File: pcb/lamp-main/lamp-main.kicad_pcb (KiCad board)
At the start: 2 copper layers, 29 parts, among them IC1 ATMEGA328P, IC2 DNP(LM1117_3.3), P1 VLED_IN, P10 VCC, P2 AVR_ISP, P3 SERIAL, P4 LEDSTACK, P5 LEDSTACK, P6 LEDSTACK, P7 USER-INPUT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

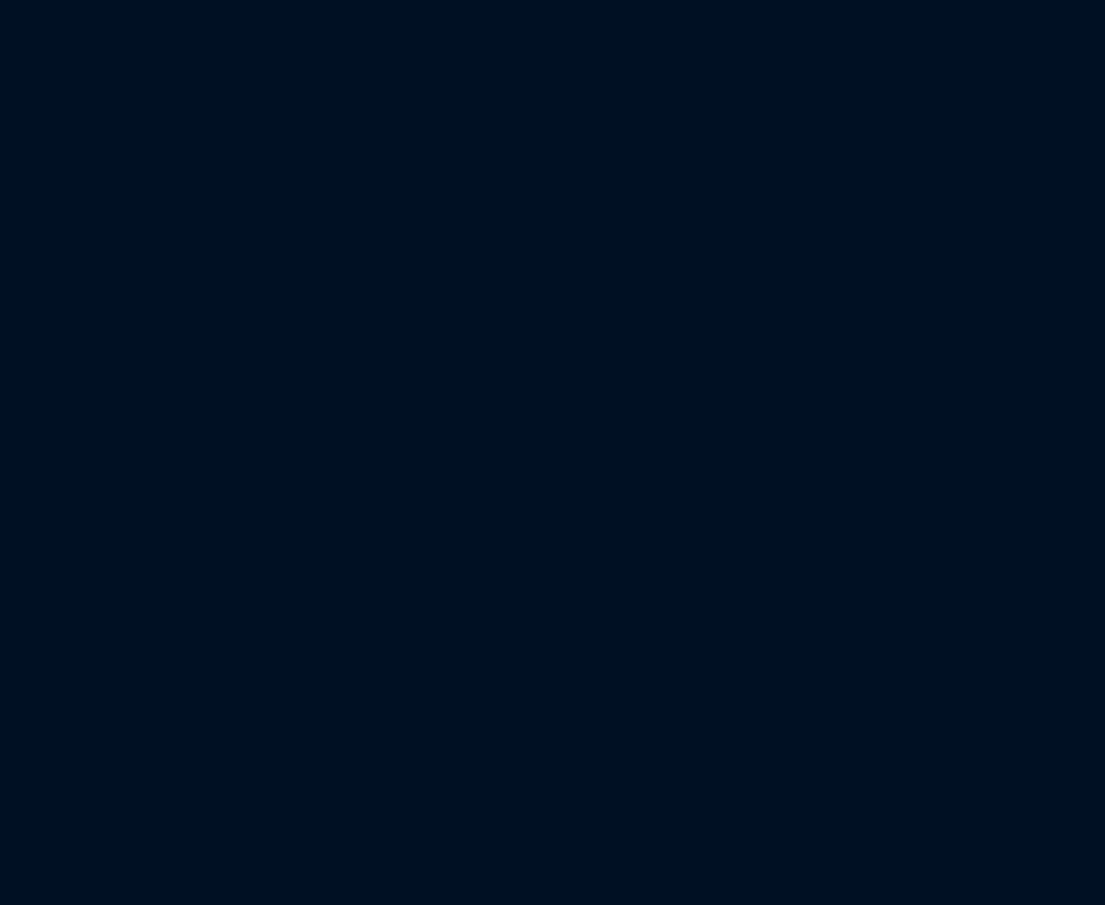
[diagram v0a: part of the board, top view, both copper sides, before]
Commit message: add board outline
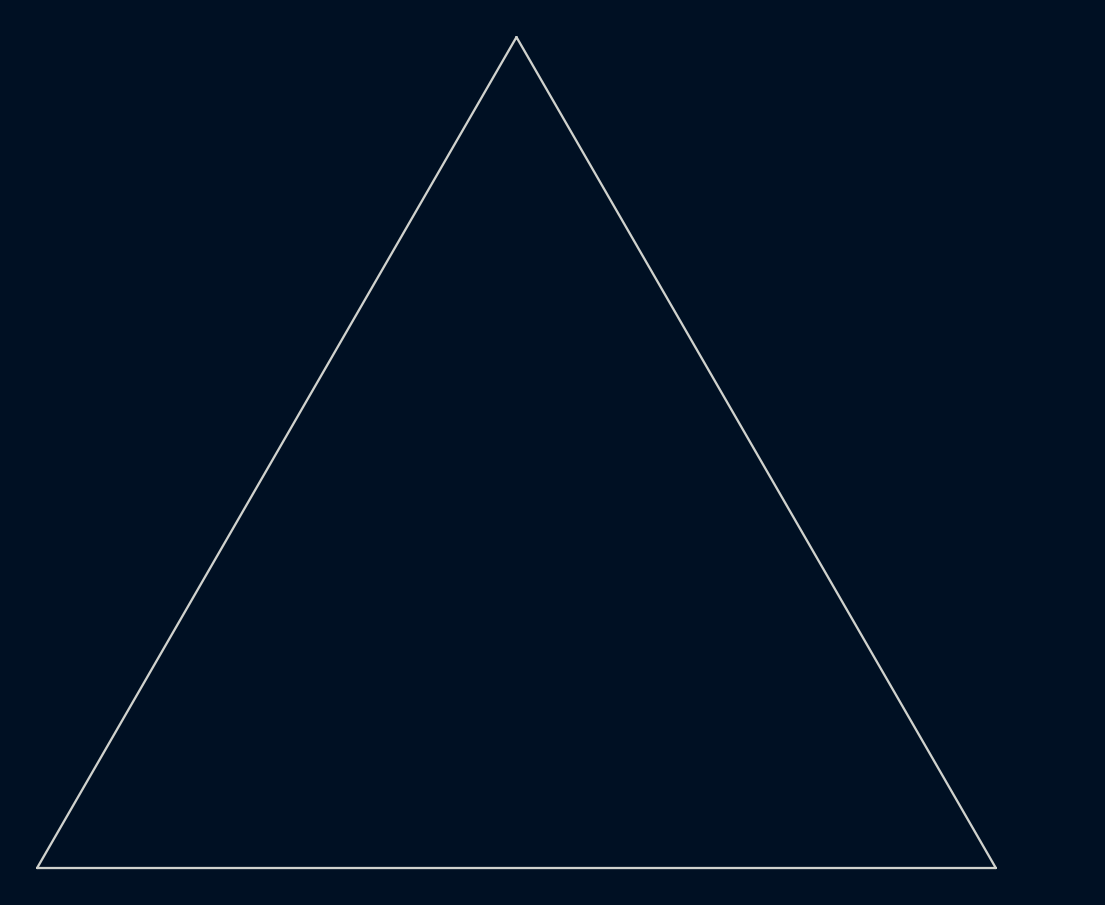
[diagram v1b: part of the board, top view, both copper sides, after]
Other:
- board outline added: 53.3 x 46.2 mm
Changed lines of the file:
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@@
     (links 79)
     (no_connects 79)
-    (area 0 0 0 0)
+    (area 115.166627 93.98 202.232686 123.255601)
     (thickness 1.6)
-    (drawings 0)
+    (drawings 3)
     (tracks 0)
     (zones 0)
@@
       (net 3 "Net-(C2-Pad2)"))
   )
+  (gr_line (start 77.47 80.772) (end 104.14 127) (angle 90) (layer Edge.Cuts) (width 0.127))
+  (gr_line (start 50.8 127) (end 77.47 80.772) (angle 90) (layer Edge.Cuts) (width 0.127))
+  (gr_line (start 50.8 127) (end 104.14 127) (angle 90) (layer Edge.Cuts) (width 0.127))
 )

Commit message: trying something new
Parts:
- moved C8 142.9 mm to (58.4, 122.0)
- moved IC2 129.3 mm to (62.2, 117.0), turned to 180 degrees
- moved C1 127.0 mm to (72.1, 115.1), turned to 225 degrees
- moved LED1 116.7 mm to (82.2, 117.1), turned to 180 degrees
- moved R6 115.4 mm to (82.2, 115.4), turned to 180 degrees
- moved P10 114.5 mm to (58.4, 125.1)
- moved C7 112.8 mm to (66.0, 122.0), turned to 180 degrees
- moved P5 112.2 mm to (65.8, 104.9), turned to 240 degrees
- moved P1 112.0 mm to (66.0, 125.1), turned to 180 degrees
- moved C4 104.5 mm to (73.4, 116.3), turned to 225 degrees
- moved C5 99.9 mm to (84.2, 107.4)
- moved P2 92.0 mm to (94.0, 118.7)
- moved P4 86.4 mm to (77.5, 125.1)
- moved P3 73.8 mm to (94.0, 125.1)
- moved P6 71.2 mm to (89.2, 104.9), turned to 120 degrees
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
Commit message: board layout and schematic refinement
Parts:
- removed P9: WIFI, sip:SIP3
- added JP1: VLED-VIN-JUMP, jumper:SOLDER-JUMPER_1-WAY, F.Cu at (69.8, 121.9)
- P10: value VCC -> V_IN
- P8: value EXTRA-IO -> EXTRA-ADC
- moved R2 117.9 mm to (66.0, 110.5)
- moved C6 115.8 mm to (81.7, 105.9), turned to 315 degrees
- moved R1 110.1 mm to (84.5, 98.4), turned to 180 degrees
- moved P8 106.3 mm to (86.4, 110.5), turned to 270 degrees
- moved R3 104.2 mm to (86.4, 122.6), turned to 180 degrees
- moved R7 100.8 mm to (86.4, 120.7), turned to 180 degrees
- moved LED2 98.1 mm to (89.5, 122.6)
- moved P7 97.6 mm to (77.5, 102.2), turned to 180 degrees
- moved C9 92.0 mm to (99.1, 121.9), turned to 270 degrees
- moved C5 2.17 mm to (83.4, 105.4), turned to 135 degrees
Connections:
- IC1 pad 1: /BUTTON_0 -> /BUTTON_1
- IC1 pad 13: /WIFI_EN -> Net-(IC1-Pad13)
- IC1 pad 14: /WIFI_SS -> Net-(IC1-Pad14)
- IC1 pad 19: /POT_1 -> /ADC6
- IC1 pad 2: /BUTTON_1 -> Net-(IC1-Pad2)
- IC1 pad 22: /POT_2 -> /ADC7
- IC1 pad 26: /ADC_C3 -> /POT_0
- IC1 pad 27: /ADC_C4 -> /POT_1
- IC1 pad 28: /POT_0 -> /POT_2
- IC1 pad 32: /WIFI_IRQ -> /BUTTON_0
- P1 pad 1: /VIN -> /VL
- P10 pad 1: VCC -> /VIN
- P4 pad 1: /VIN -> /VL
- P5 pad 1: /VIN -> /VL
- P6 pad 1: /VIN -> /VL
- P8 pad 1: /ADC_C3 -> /ADC7
- P8 pad 2: /ADC_C4 -> /ADC6

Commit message: still working on the layout
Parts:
- moved R3 21.1 mm to (104.1, 111.1)
- moved P7 17.3 mm to (87.6, 116.2), turned to 270 degrees
- moved R7 16.3 mm to (99.1, 110.5)
- moved P8 15.4 mm to (98.4, 101.0)
- moved LED2 15.3 mm to (103.5, 116.2)
- moved P1 8.26 mm to (58.4, 121.9)
- moved C8 8.15 mm to (61.0, 114.3), turned to 225 degrees
- moved IC2 3.81 mm to (66.0, 116.8), turned to 45 degrees
- moved C7 3.05 mm to (66.0, 125.1), turned to 0 degrees
- moved JP1 1.27 mm to (68.6, 121.9), turned to 180 degrees
- turned P10 to 180 degrees
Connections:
- net /BUTTON_1 renamed /WIFI_IRQ

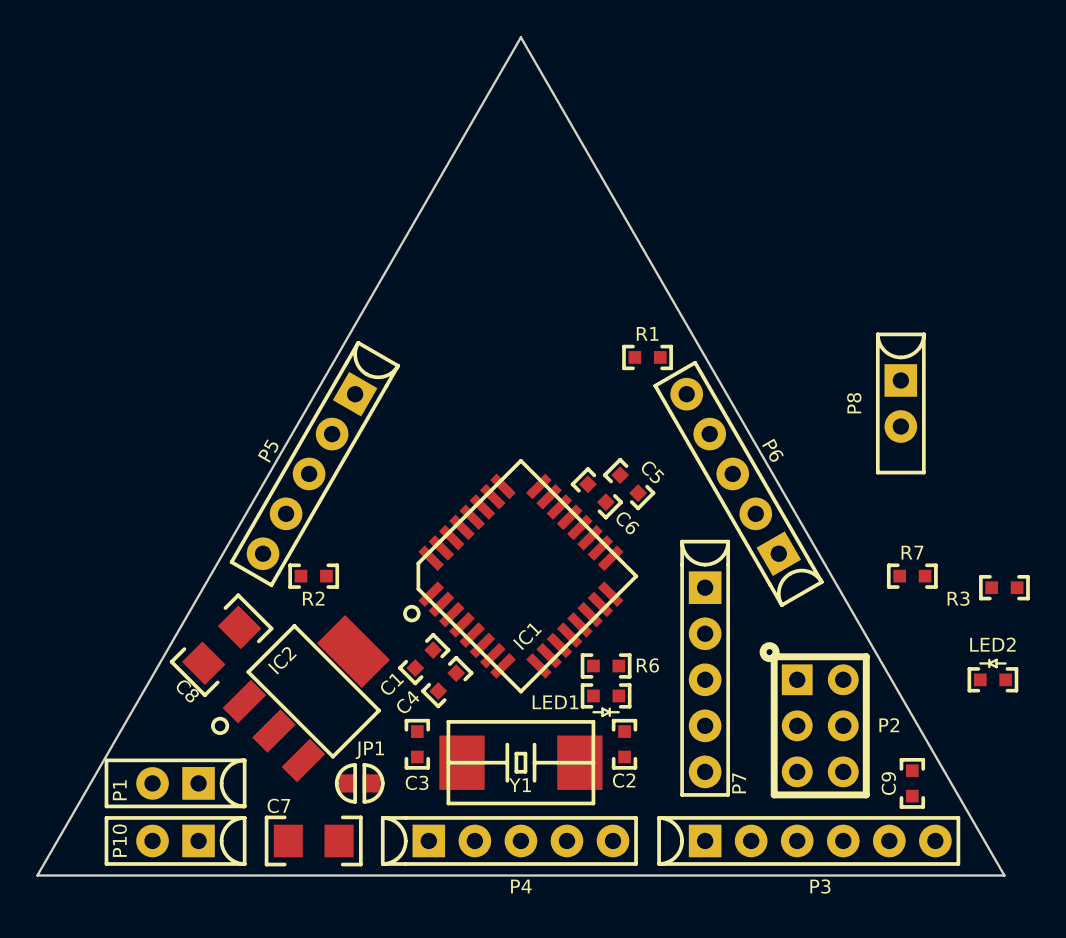
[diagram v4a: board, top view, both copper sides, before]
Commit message: wire up main board
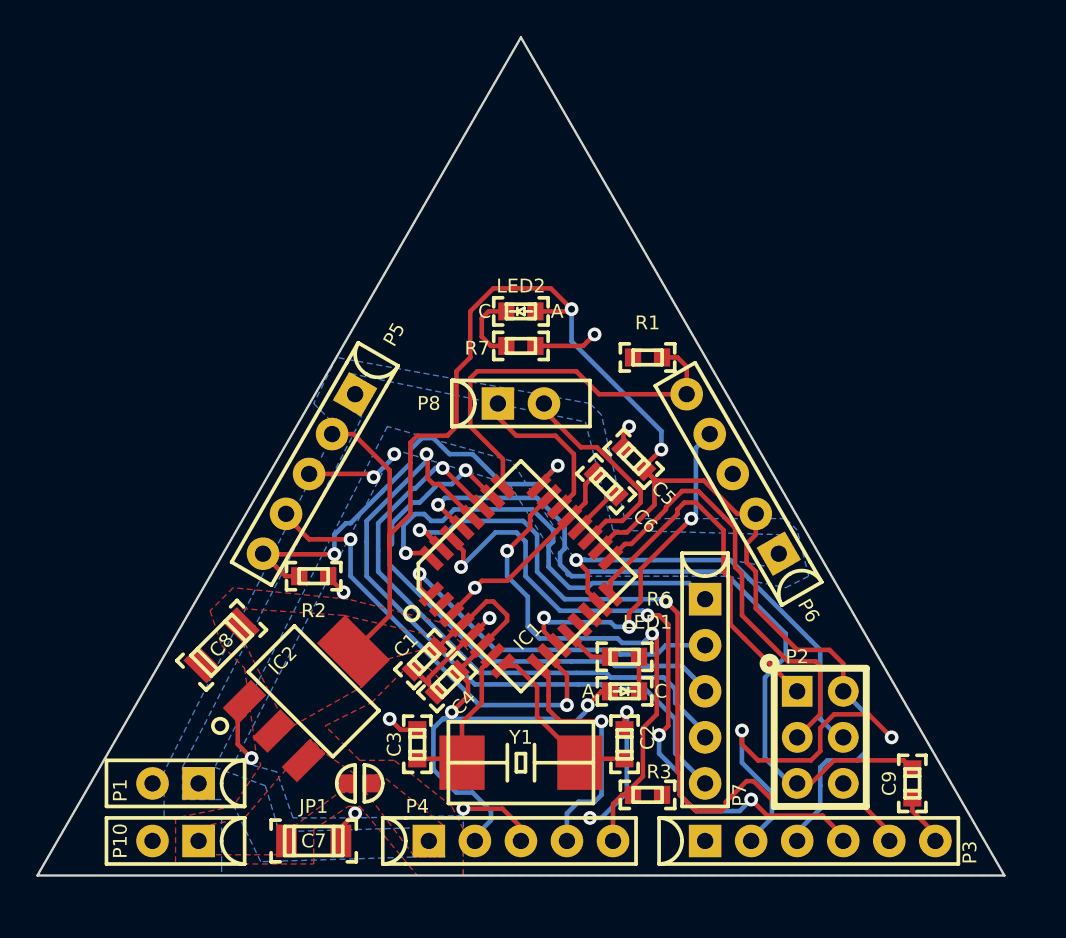
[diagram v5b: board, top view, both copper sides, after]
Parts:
- C1, C2, C3, C4, C5, C6, C9: footprint passive-smd:0603(1608m) -> capacitor:0603(1608m)-CHIP-CAP
- C7, C8: footprint passive-smd:1206(3216m) -> capacitor:1206(3216m)-CHIP-CAP
- R1, R2, R3, R6, R7: footprint passive-smd:0603(1608m) -> resistor:0603(1608m)-CHIP-RESISTOR
- moved LED2 33.0 mm to (77.5, 95.9)
- moved R7 25.0 mm to (77.5, 97.8), turned to 0 degrees
- moved R3 22.8 mm to (84.5, 122.6), turned to 0 degrees
- moved P8 21.0 mm to (77.5, 101.0), turned to 0 degrees
- moved C5 1.42 mm to (83.7, 104.0)
- moved R6 1.14 mm to (83.2, 114.9)
- moved LED1 1.05 mm to (83.2, 116.8)
- moved C6 0.72 mm to (82.2, 105.4)
- moved P7 0.64 mm to (87.6, 116.8)
- moved P2 0.63 mm to (94.0, 119.4)
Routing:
- net VCC: track 0.00 -> 122.3 mm, vias 0 -> 4
- net GND: track 0.00 -> 68.9 mm, vias 0 -> 15
- net /USART_TX: track 0.00 -> 45.6 mm, vias 0 -> 2
- net /AVR_RST: track 0.00 -> 43.1 mm, vias 0 -> 1
- net /USART_RX: track 0.00 -> 38.2 mm, vias 0 -> 4
- net /POT_2: track 0.00 -> 37.7 mm, vias 0 -> 1
- net /POT_1: track 0.00 -> 33.2 mm, vias 0 -> 1
- net /POT_0: track 0.00 -> 30.3 mm, vias 0 -> 1
- net /STACKSENSE0: track 0.00 -> 28.9 mm, vias 0 -> 2
- net /STACKSENSE1: track 0.00 -> 25.6 mm, vias 0 -> 2
- net /AVR_MOSI: track 0.00 -> 24.4 mm, vias 0 -> 1
- net /AVR_SCK: track 0.00 -> 24.3 mm
- net /LEDSTACK1: track 0.00 -> 24.3 mm, vias 0 -> 2
- net /BUTTON_0: track 0.00 -> 24.2 mm, vias 0 -> 1
- net /STACKSENSE2: track 0.00 -> 22.4 mm
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- added copper zone on F.Cu, net /VIN
- added copper zone on B.Cu, net /VL
- added copper zone on F.Cu, net /VL
- added copper zone on B.Cu, net GND
- added copper zone on F.Cu, net GND
- added copper zone on F.Cu, net VCC
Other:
- net class Default: via_dia 0.889 -> 0.762; via_drill 0.635 -> 0.381
- rule trace_min: 0.254 -> 0.1524
- rule via_min_drill: 0.508 -> 0.3302
- rule via_min_size: 0.889 -> 0.6858
